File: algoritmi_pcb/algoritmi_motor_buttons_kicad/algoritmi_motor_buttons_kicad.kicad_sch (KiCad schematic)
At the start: 19 parts, among them J1 TSM-105-01-F-SH, U1 MT6701-CT

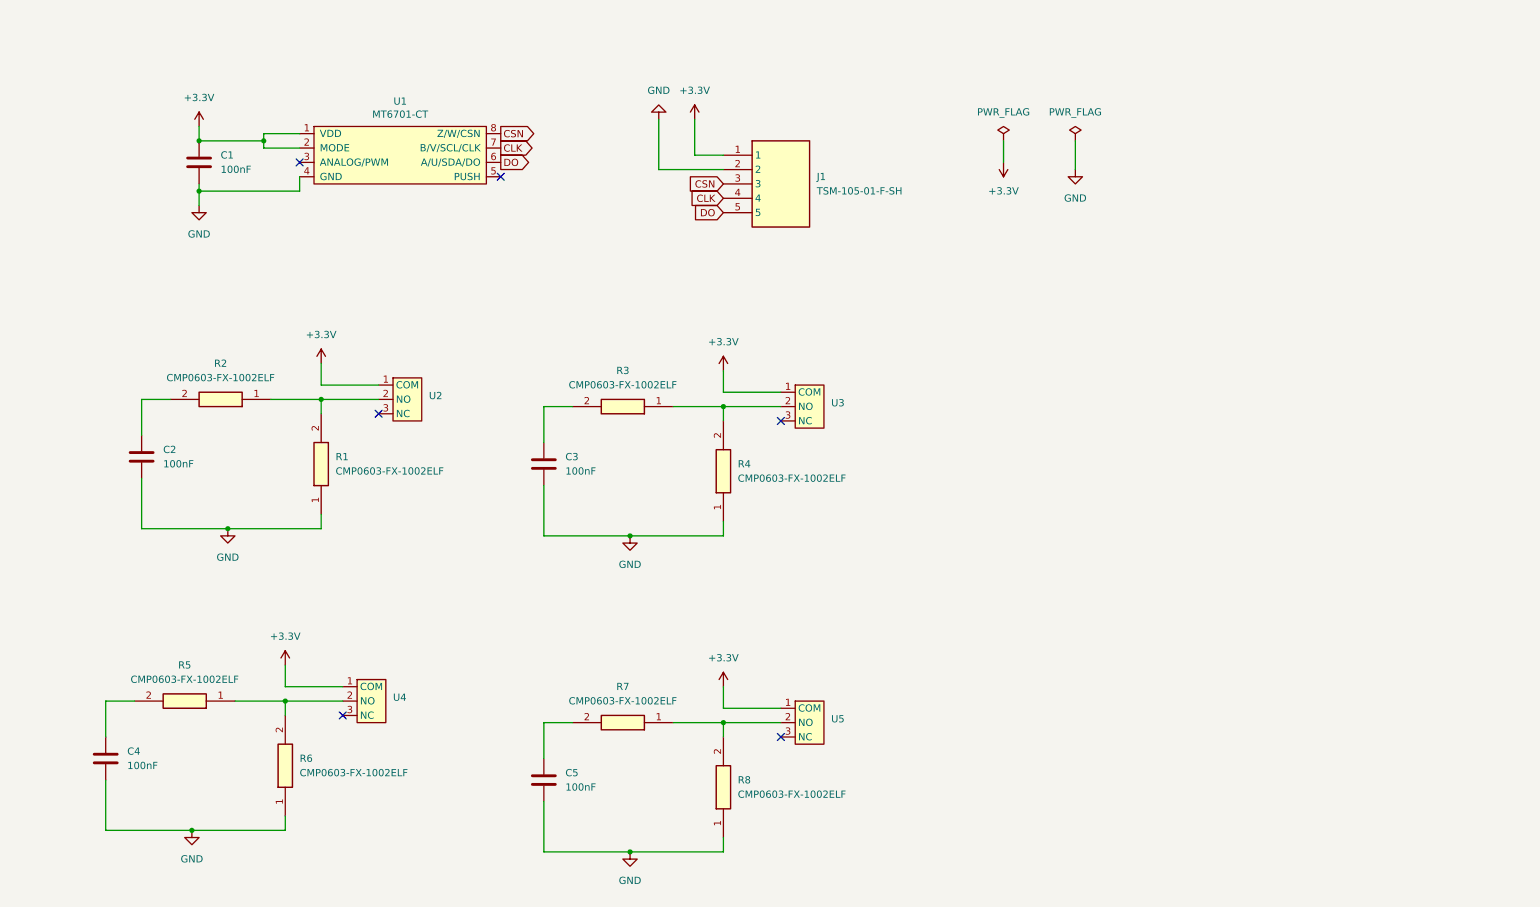
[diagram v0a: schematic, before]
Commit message: generated BOMs and Gerbers
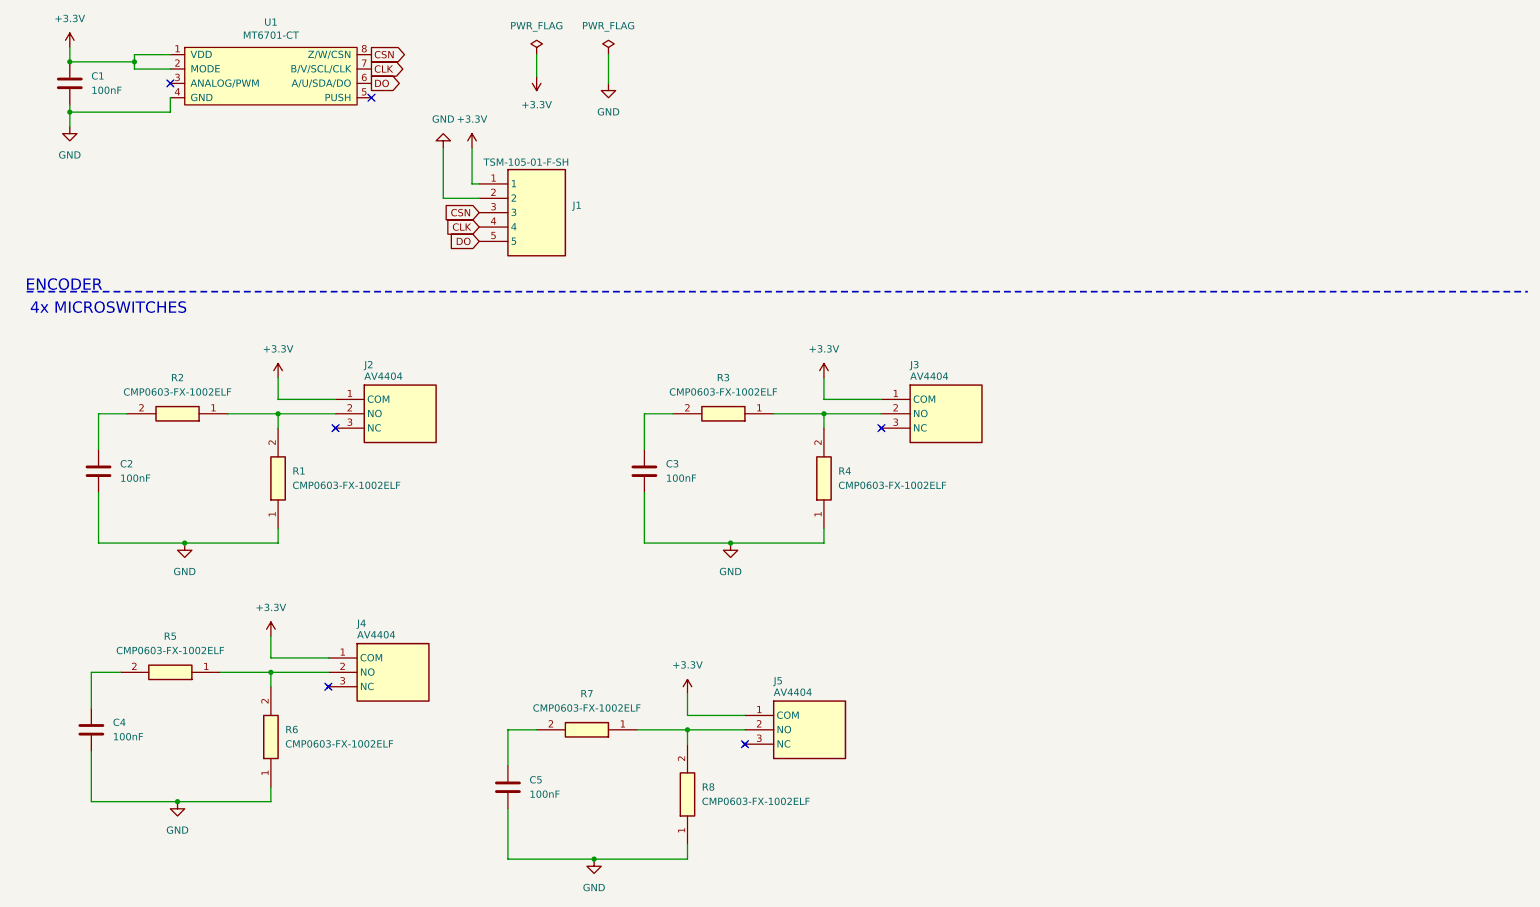
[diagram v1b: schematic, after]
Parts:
- removed U2, U3, U4, U5: ~, SamacSys_Parts:microswitch, symbol SamacSys_Parts:microswitch
- added J2, J3, J4, J5: AV4404, AV4404, symbol SamacSys_Parts:AV4404
- U1: LCSC C2856764, or C3003196 -> C2856764 ou C3003196
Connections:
- net +3.3V: now also J2.1 (COM), J3.1 (COM), J4.1 (COM), J5.1 (COM)
- net at R3.1, R4.2: now also J3.2 (NO)
- net at R7.1, R8.2: now also J5.2 (NO)
- net at R5.1, R6.2: now also J4.2 (NO)
- net at R1.2, R2.1: now also J2.2 (NO)
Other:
- note added: "4x MICROSWITCHES"
- note added: "ENCODER"
- company: (none) -> Universidade do Minho
- title: (none) -> algoritmi_foc_motor
- moved on the sheet: C1, C2, C3, C4, C5, J1, R1, R2, R3, R4, R5, R6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
